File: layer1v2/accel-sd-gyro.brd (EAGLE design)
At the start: 17.8 x 49.5 mm, 17 parts, among them IC2 LGD20H, U1 MMA8452Q, U2 microSD

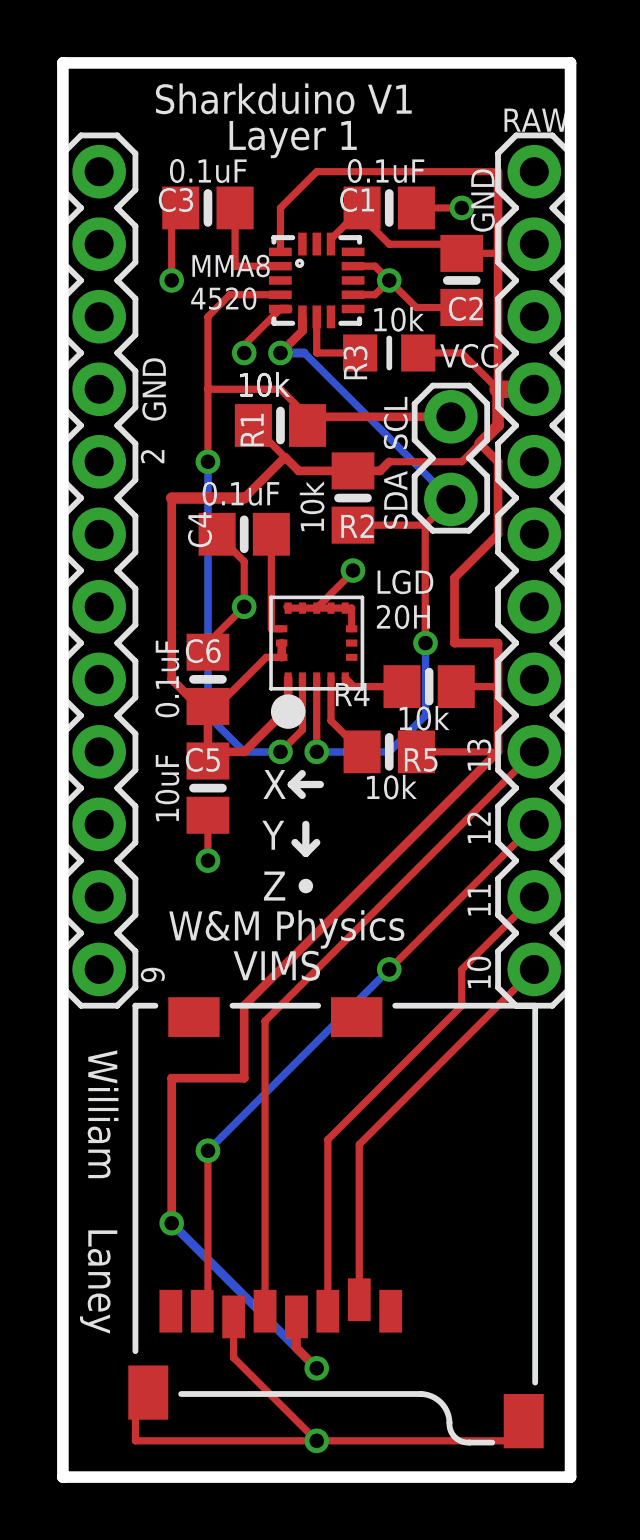
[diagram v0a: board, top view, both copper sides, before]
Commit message: removed via under sd
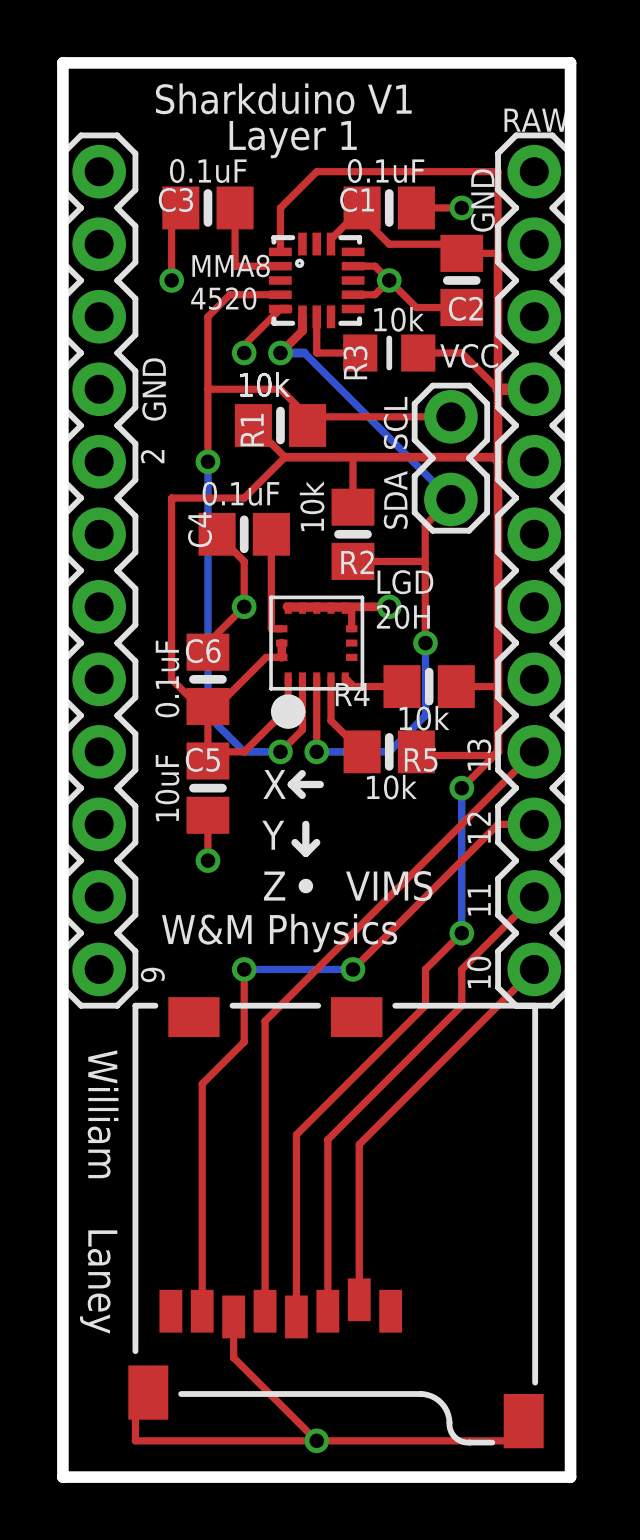
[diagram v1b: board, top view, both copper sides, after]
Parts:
- moved R2 1.27 mm to (10.2, 33.0)
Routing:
- net +3V3: track 113.1 -> 103.0 mm
- net MISO: track 22.0 -> 25.0 mm
- net GND: track 46.1 -> 47.9 mm
